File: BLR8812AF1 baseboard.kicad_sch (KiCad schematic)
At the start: 30 parts, among them Q1 AO3401A, U1 USBLC6-2SC6, U2 BL-R8812AF1, U3 TPS82130, X1 TYPE-C-31-M-12

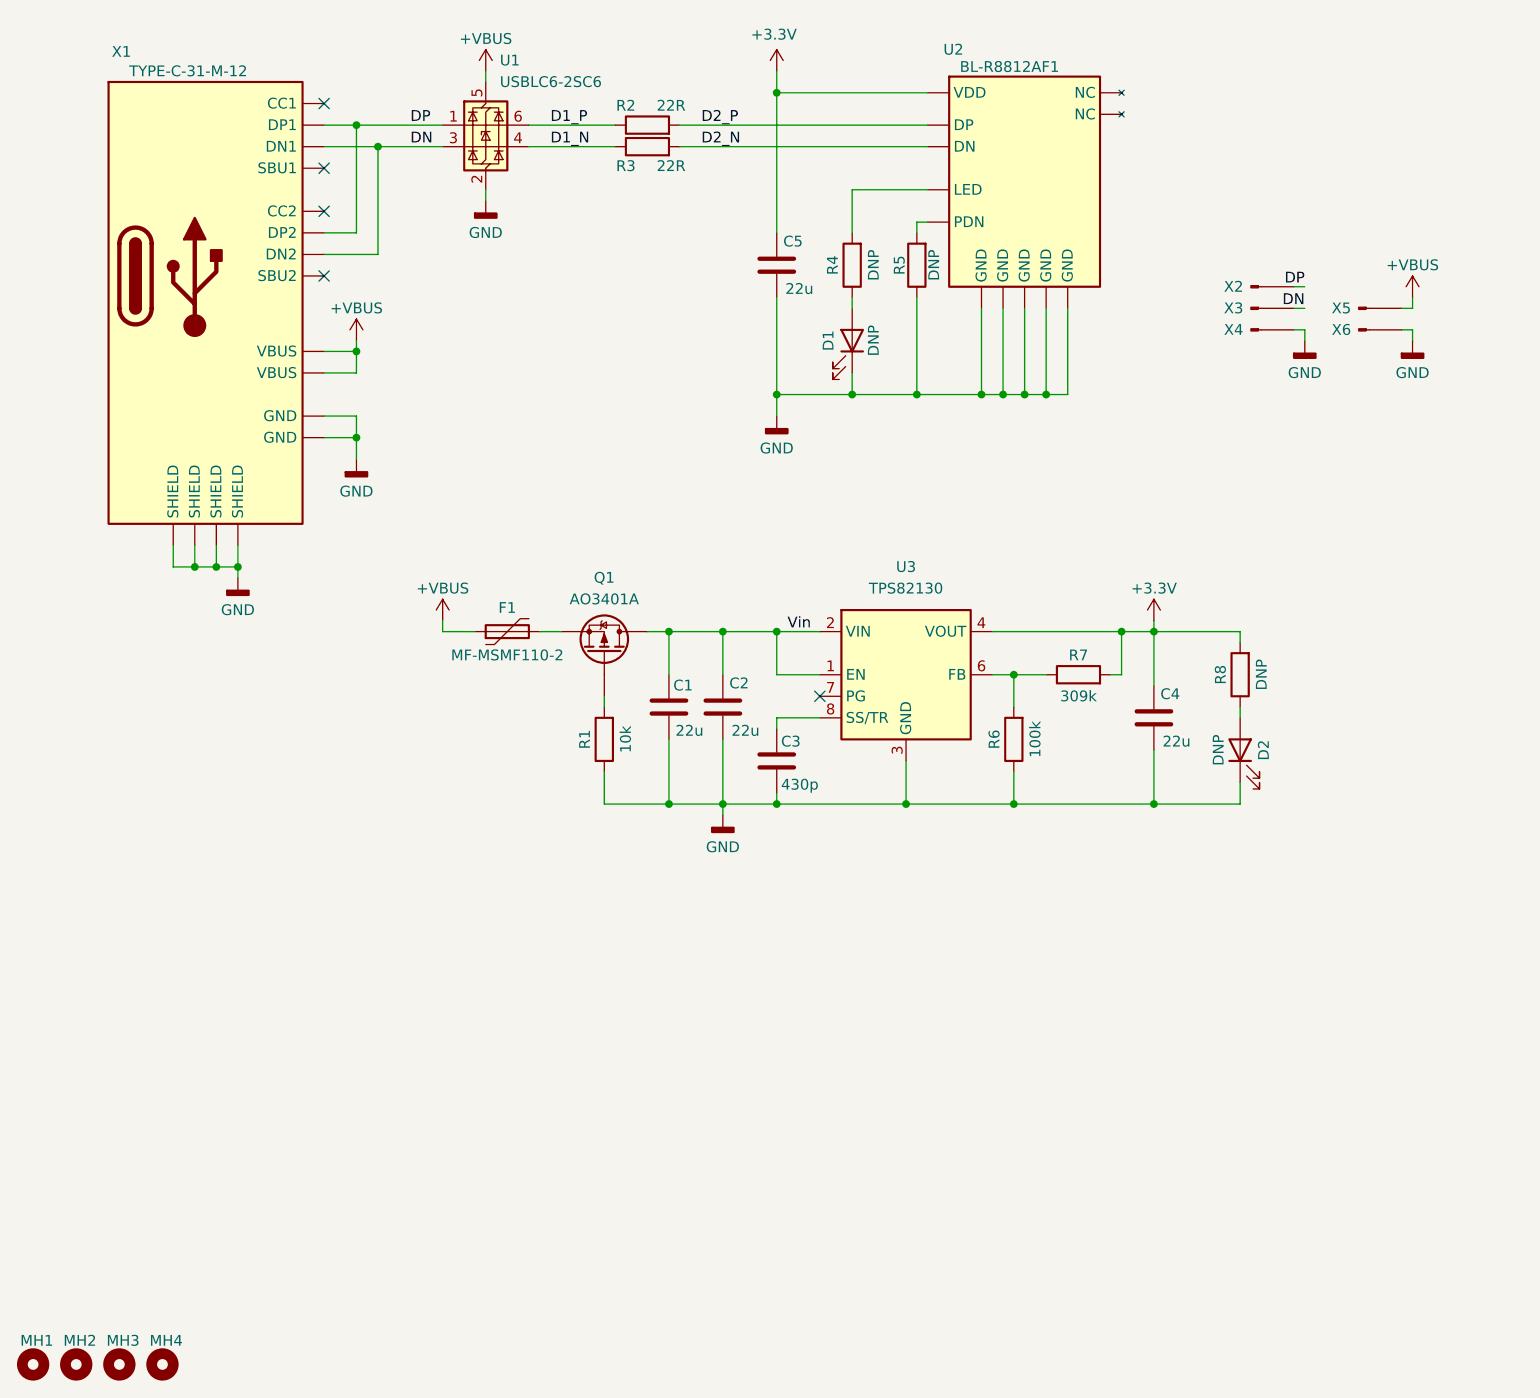
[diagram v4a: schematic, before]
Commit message: Done placing and routing, need to add stiching vias
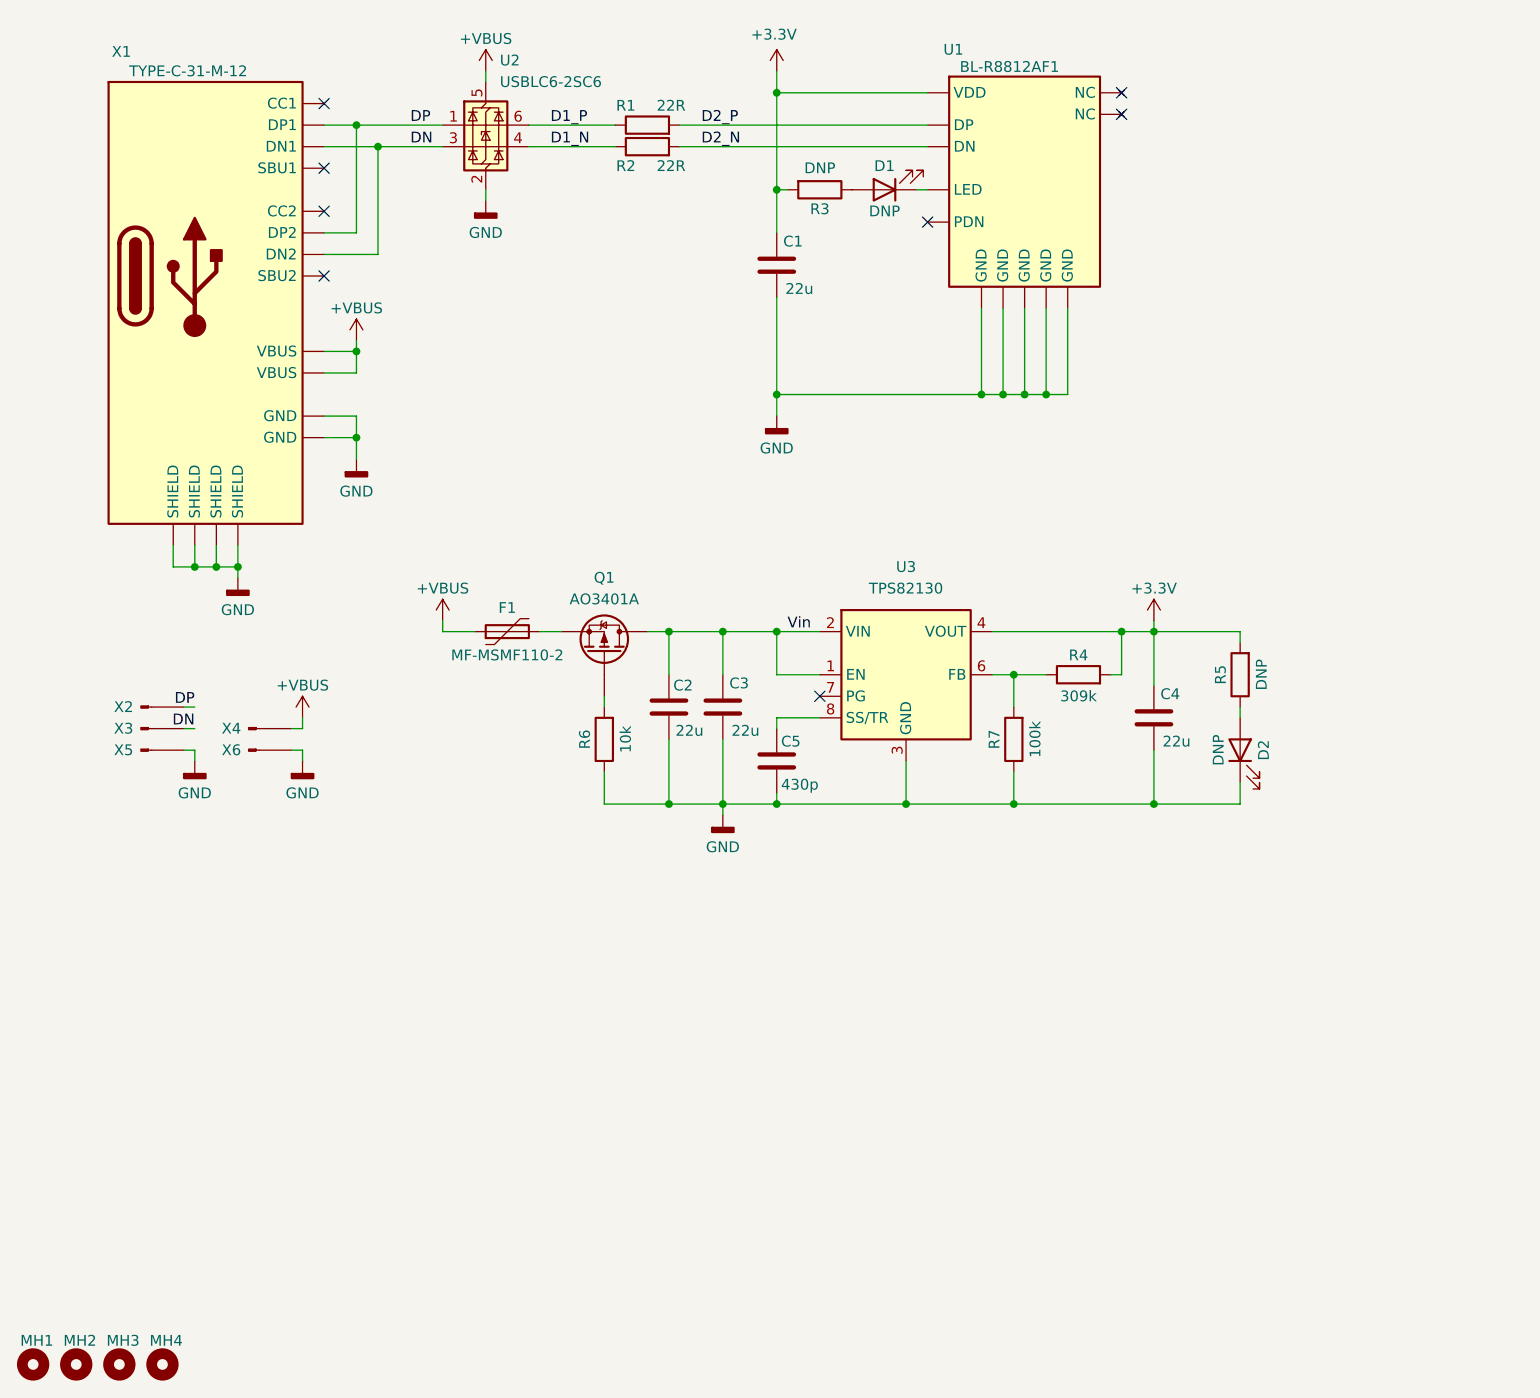
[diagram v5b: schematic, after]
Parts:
- removed R5: DNP, Resistor_SMD:R_0402_1005Metric, symbol Device:R
- renumbered C5 to C1, C1 to C2, C2 to C3, C3 to C5, R2 to R1, R3 to R2, R4 to R3, R7 to R4, R8 to R5, R1 to R6, R6 to R7, U2 to U1, U1 to U2, X5 to X4, X4 to X5
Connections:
- net +3.3V: now also R3.2
- net GND: no longer D1.1 (K)
- net at U1.6 (LED): now also D1.1 (K); no longer R3.2
- no-connect marks 5 -> 8
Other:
- moved on the sheet: D1, R3, X2, X3, X4, X5, X6

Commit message: PCB done
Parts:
- R3, R5: value DNP -> 1k
- U3: footprint Package_LGA:Texas_SIL0008D_MicroSiP-8-1EP_2.8x3mm_P0.65mm_EP1.1x1.9mm_ThermalVias -> Package_LGA:Texas_SIL0008D_MicroSiP-8-1EP_2.8x3mm_P0.65mm_EP1.1x1.9mm
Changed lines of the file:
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@@
 		(dnp no)
 		(property "Reference" "R3"
-			(at 120.65 48.006 90)
-			(effects
-				(font
-					(size 1.27 1.27)
-				)
-			)
-		)
-		(property "Value" "DNP"
-			(at 120.65 43.18 90)
+			(at 120.65 43.434 90)
+			(effects
+				(font
+					(size 1.27 1.27)
+				)
+			)
+		)
+		(property "Value" "1k"
+			(at 120.65 48.26 90)
 			(effects
 				(font
@@
 			)
 		)
-		(property "Footprint" "Package_LGA:Texas_SIL0008D_MicroSiP-8-1EP_2.8x3mm_P0.65mm_EP1.1x1.9mm_ThermalVias"
+		(property "Footprint" "Package_LGA:Texas_SIL0008D_MicroSiP-8-1EP_2.8x3mm_P0.65mm_EP1.1x1.9mm"
 			(at 130.81 119.38 0)
 			(effects
@@
 			)
 		)
-		(property "Value" "DNP"
-			(at 172.72 102.87 90)
-			(effects
-				(font
+		(property "Value" "1k"
+			(at 172.466 102.87 90)
+			(effects
+				(font

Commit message: Fixed reverce voltage protection
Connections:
- net Vin: now also Q1.2 (S); no longer Q1.3 (D)
- net at F1.2: now also Q1.3 (D); no longer Q1.2 (S)
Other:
- moved on the sheet: Q1
